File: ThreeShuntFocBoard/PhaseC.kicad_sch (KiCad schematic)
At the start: 40 parts, among them J10 Conn_01x01, Q1 MMBT5551L, Q10 IRF540N, Q2 SS8050, Q3 SS8550, Q4 SS8550, Q5 SS8550, Q6 SS8550, Q7 IRF540N, Q8 IRF540N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

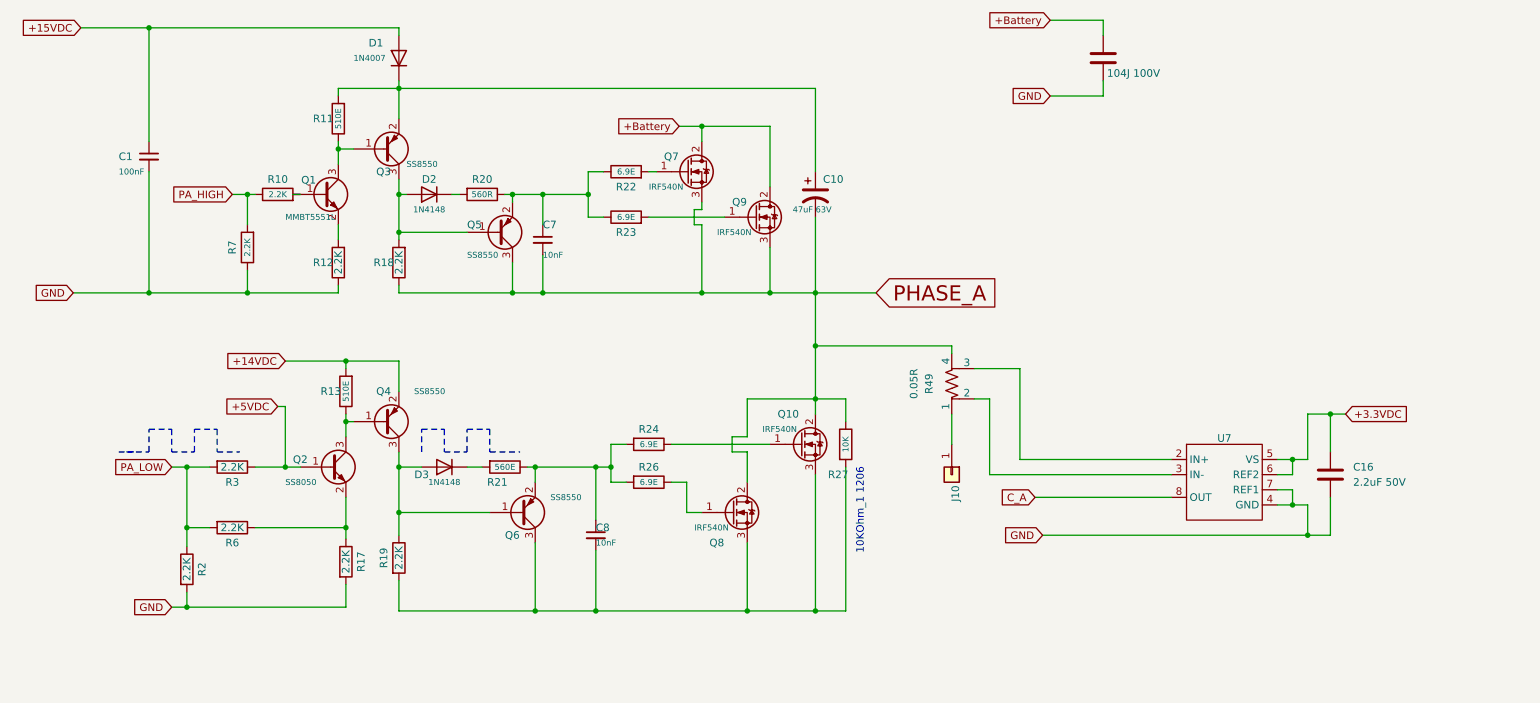
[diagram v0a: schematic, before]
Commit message: commit 2:  Updated Power Supply, Safety Fuse, Phase Design, and Hall Sensor Circuit
for more details read ChangesDetial.txt in same folder.
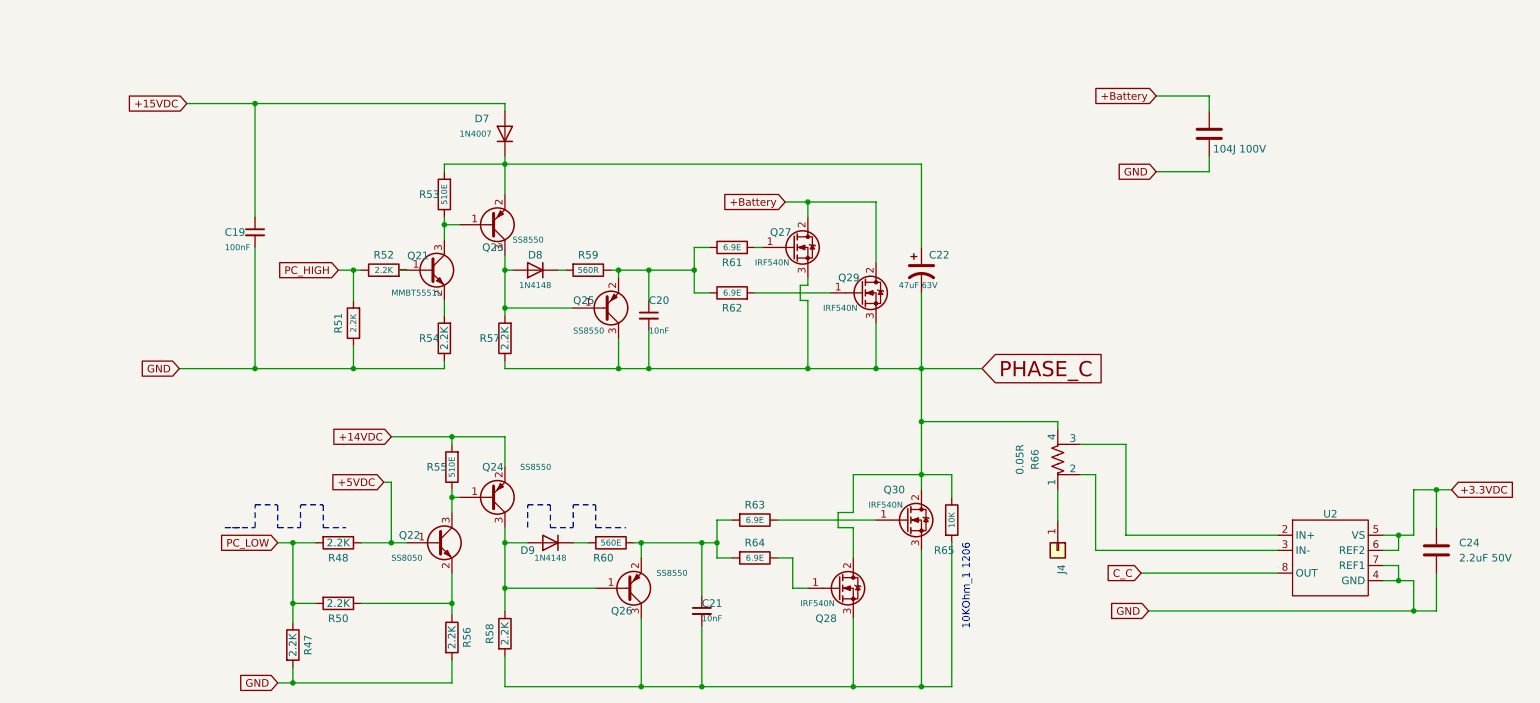
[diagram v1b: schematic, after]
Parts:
- removed C1: 100nF, Footprints:C_0603, symbol Device:C_Small
- removed C10: 47uF 63V, BLDC:220uF63V, symbol Device:C_Polarized_US
- removed C11: 104J 100V, Footprints:104J_100V, symbol Device:C
- removed C16: 2.2uF 50V, symbol Device:C
- removed C7, C8: 10nF, Footprints:C_0603, symbol Device:C_Small
- removed D1: 1N4007, BLDC:ZenerDiode_S1M, symbol Diode:1N4007
- removed D2, D3: 1N4148, Footprints:SOD_123_v1, symbol Diode:1N4148
- removed J10: Conn_01x01, Footprints:Powe_pad, symbol Connector_Generic:Conn_01x01
- removed Q1: MMBT5551L, Footprints:SOT-23_v1, symbol Transistor_BJT:MMBT5551L
- removed Q10, Q7, Q8, Q9: IRF540N, BLDC:TO-220-3_Vertical, symbol Transistor_FET:IRF540N
- removed Q2: SS8050, Footprints:SOT-23_v1, symbol Transistor_BJT:S8050
- removed Q3, Q4, Q5, Q6: SS8550, Footprints:SOT-23_v1, symbol Transistor_BJT:S8550
- removed R10, R12, R17, R18, R19, R2, R3, R6, R7: 2.2K, Footprints:R_0603, symbol Device:R
- removed R11, R13: 510E, Footprints:R_0603, symbol Device:R
- removed R20: 560R, Footprints:R_0603, symbol Device:R
- removed R21: 560E, Footprints:R_0603, symbol Device:R
- removed R22, R23, R24, R26: 6.9E, Footprints:R_0603, symbol Device:R
- removed R27: 10K, Footprints:1206_R, symbol Device:R
- removed R49: 0.05R, symbol Device:R_Shunt_US
- removed U7: ~, symbol Symbol_lib:INA240
- added C19: 100nF, Footprints:C_0603, symbol Device:C_Small
- added C20, C21: 10nF, Footprints:C_0603, symbol Device:C_Small
- added C22: 47uF 63V, BLDC:220uF63V, symbol Device:C_Polarized_US
- added C23: 104J 100V, Footprints:104J_100V, symbol Device:C
- added C24: 2.2uF 50V, symbol Device:C
- added D7: 1N4007, BLDC:ZenerDiode_S1M, symbol Diode:1N4007
- added D8, D9: 1N4148, Footprints:SOD_123_v1, symbol Diode:1N4148
- added J4: Conn_01x01, Footprints:Powe_pad, symbol Connector_Generic:Conn_01x01
- added Q21: MMBT5551L, Footprints:SOT-23_v1, symbol Transistor_BJT:MMBT5551L
- added Q22: SS8050, Footprints:SOT-23_v1, symbol Transistor_BJT:S8050
- added Q23, Q24, Q25, Q26: SS8550, Footprints:SOT-23_v1, symbol Transistor_BJT:S8550
- added Q27, Q28, Q29, Q30: IRF540N, BLDC:TO-220-3_Vertical, symbol Transistor_FET:IRF540N
- added R47, R48, R50, R51, R52, R54, R56, R57, R58: 2.2K, Footprints:R_0603, symbol Device:R
- added R53, R55: 510E, Footprints:R_0603, symbol Device:R
- added R59: 560R, Footprints:R_0603, symbol Device:R
- added R60: 560E, Footprints:R_0603, symbol Device:R
- added R61, R62, R63, R64: 6.9E, Footprints:R_0603, symbol Device:R
- added R65: 10K, Footprints:1206_R, symbol Device:R
- added R66: 0.05R, symbol Device:R_Shunt_US
- added U2: ~, symbol Symbol_lib:INA240
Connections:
- net +14VDC: now also Q24.2 (E), R55.2
- net +15VDC: now also C19.1, D7.2 (A)
- net +3.3VDC: now also C24.1, U2.5 (VS), U2.6 (REF2)
- net +5VDC: now also Q22.1 (B), R48.1
- net +Battery: now also C23.1, Q27.2 (D), Q29.2 (D)
- net GND: now also C19.2, C23.2, C24.2, R47.2, R51.1, R54.1, R56.2, U2.4 (GND), U2.7 (REF1)
- new net: D9.2 (A), Q24.3 (C), Q26.1 (B), R58.1
- new net: C21.1, Q26.2 (E), R60.1, R63.2, R64.2
- new net: C21.2, Q26.3 (C), Q28.3 (S), Q30.3 (S), R58.2, R65.2
- new net: Q22.2 (E), R50.1, R56.1
- new net: C20.1, Q25.2 (E), R59.1, R61.1, R62.1
- new net: Q29.1 (G), R62.2
- new net: Q22.3 (C), Q24.1 (B), R55.1
- new net: Q21.2 (E), R54.2
- new net: Q28.1 (G), R64.1
- new net: Q21.1 (B), R52.2
- new net: Q21.3 (C), Q23.1 (B), R53.1
- new net: C22.1, D7.1 (K), Q23.2 (E), R53.2
- new net: D9.1 (K), R60.2
- new net: D8.1 (K), R59.2
- new net: D8.2 (A), Q23.3 (C), Q25.1 (B), R57.2
- new net: Q30.1 (G), R63.1
- new net: J4.1 (Pin_1), R66.1
- new net: R66.3, U2.2 (IN+)
- new net: R66.2, U2.3 (IN-)
- new net: Q27.1 (G), R61.2
- new net C_C: U2.8 (OUT)
- new net PC_HIGH: R51.2, R52.1
- new net PC_LOW: R47.1, R48.2, R50.2
- new net PHASE_C: C20.2, C22.2, Q25.3 (C), Q27.3 (S), Q28.2 (D), Q29.3 (S), Q30.2 (D), R57.1, R65.1, R66.4

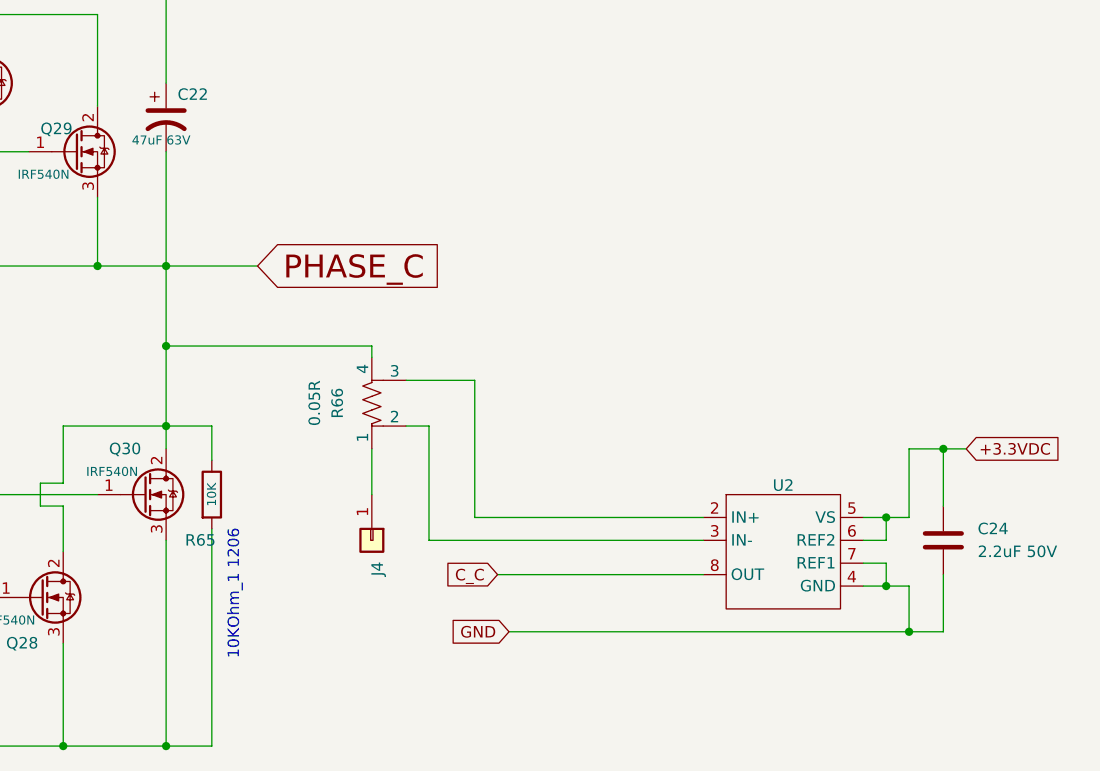
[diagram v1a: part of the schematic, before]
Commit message: Commit 3: Assigned STM32G431C6Tx (LQFP-48) pins as per the shared Excel, peripheral connections WIP, Phase C current sensing removed due to ADC group limitations
read attach excel files and changesDetails.txt file for more detail
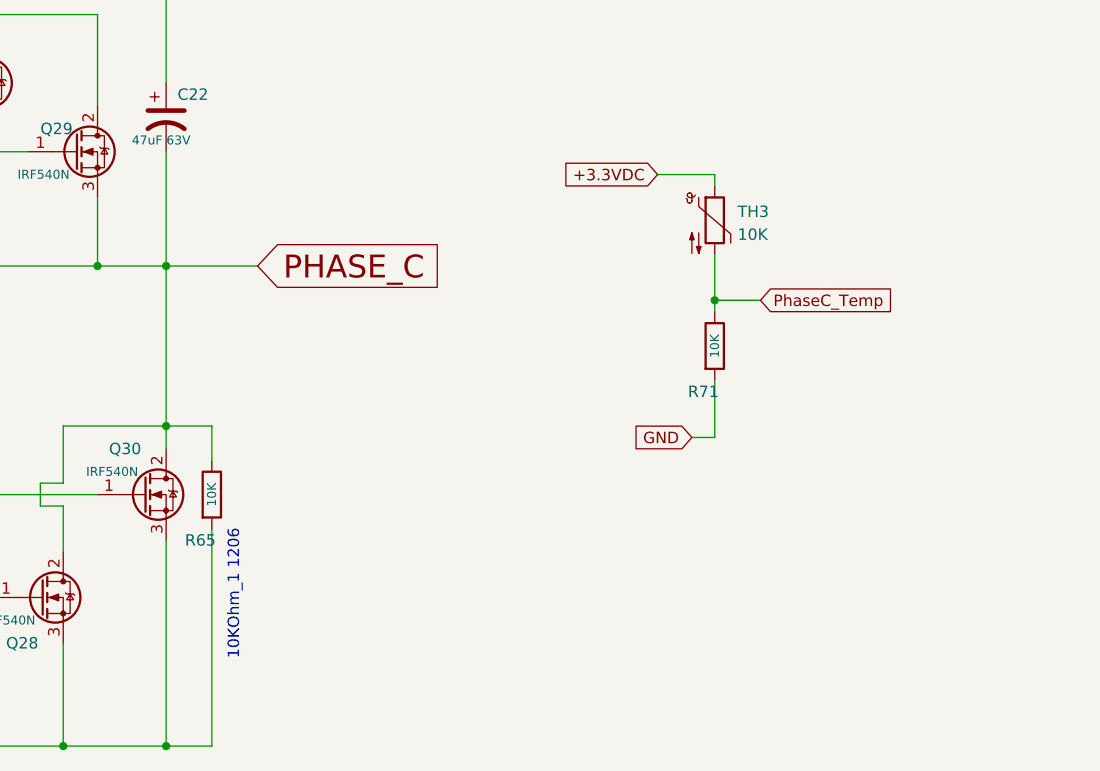
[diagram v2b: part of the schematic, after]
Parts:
- removed C24: 2.2uF 50V, symbol Device:C
- removed J4: Conn_01x01, Footprints:Powe_pad, symbol Connector_Generic:Conn_01x01
- removed R66: 0.05R, symbol Device:R_Shunt_US
- removed U2: ~, symbol Symbol_lib:INA240
- added R71: 10K, Footprints:1206_R, symbol Device:R
- added TH3: 10K, symbol Device:Thermistor_NTC
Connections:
- net +3.3VDC: now also TH3.1
- net GND: now also R71.2
- new net PhaseC_Temp: R71.1, TH3.2
